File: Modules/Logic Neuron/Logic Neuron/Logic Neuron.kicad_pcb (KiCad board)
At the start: 2 copper layers, 123.1 x 128.5 mm, 122 parts, among them J1 PJ301M-12, J10 PJ301M-12, J11 EURO_PWR_2x5, J2 PJ301M-12, J3 PJ301M-12, J4 PJ301M-12, J5 Conn_01x04, J6 Conn_01x04, J7 PJ301M-12, J8 PJ301M-12, J9 PJ301M-12, U1 TL074, U2 LM339, U3 TL074, U4 TL074, U5 LM79L05_TO92, U9 LM339

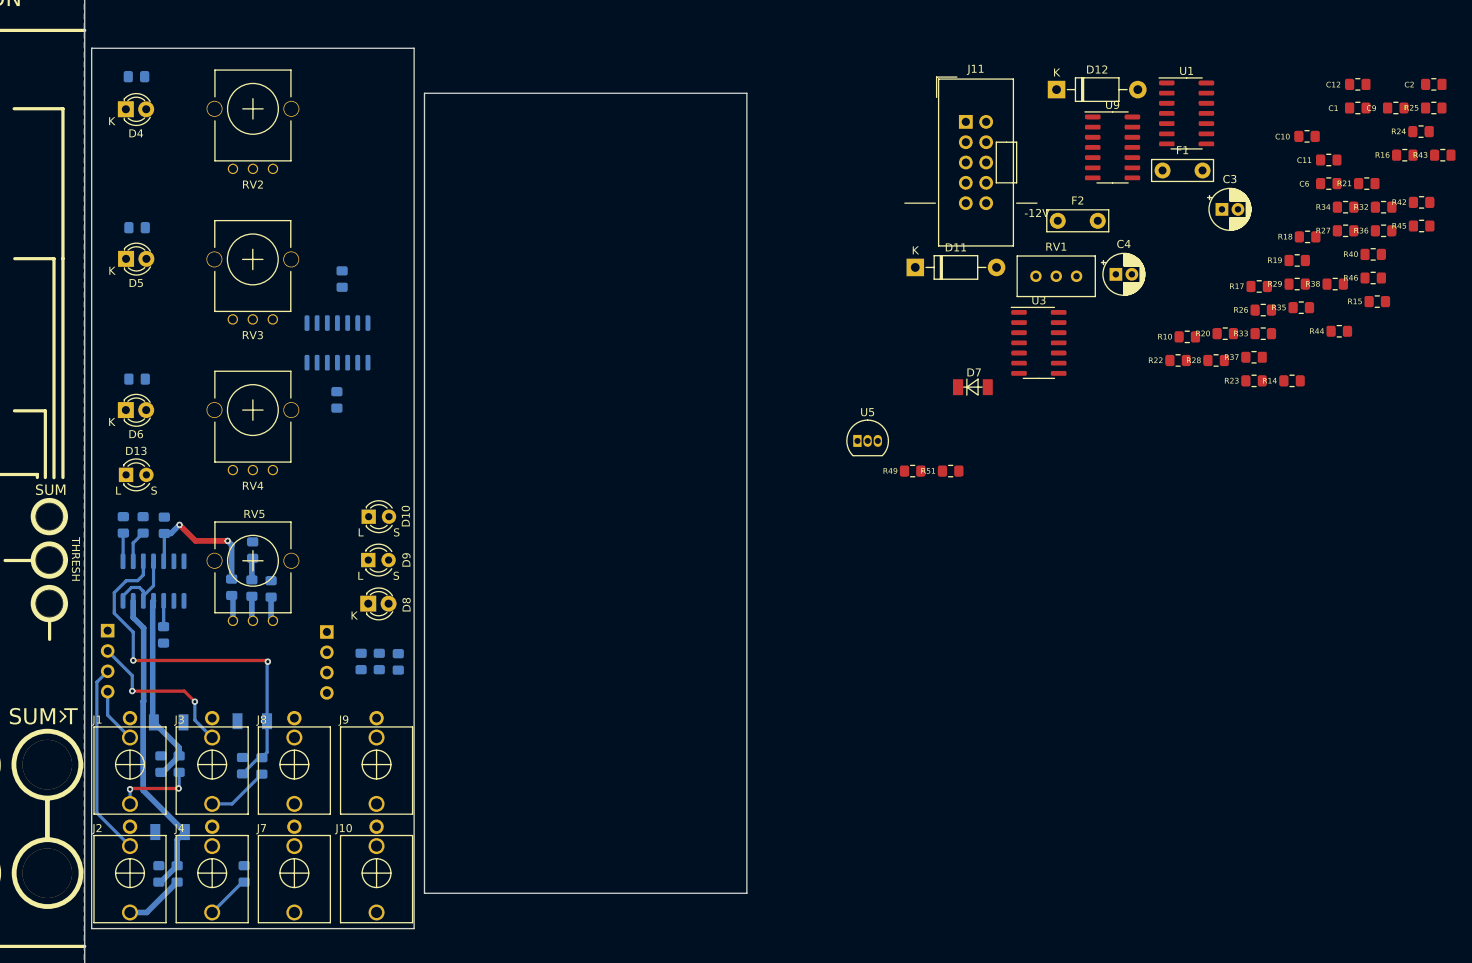
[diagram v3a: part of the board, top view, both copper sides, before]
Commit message: Logic Neuron : PCB routing
Logic Neuron: First pass of PCB routing almost completed.

To do:
- ground planes
- DRCs
- silkscreen markings
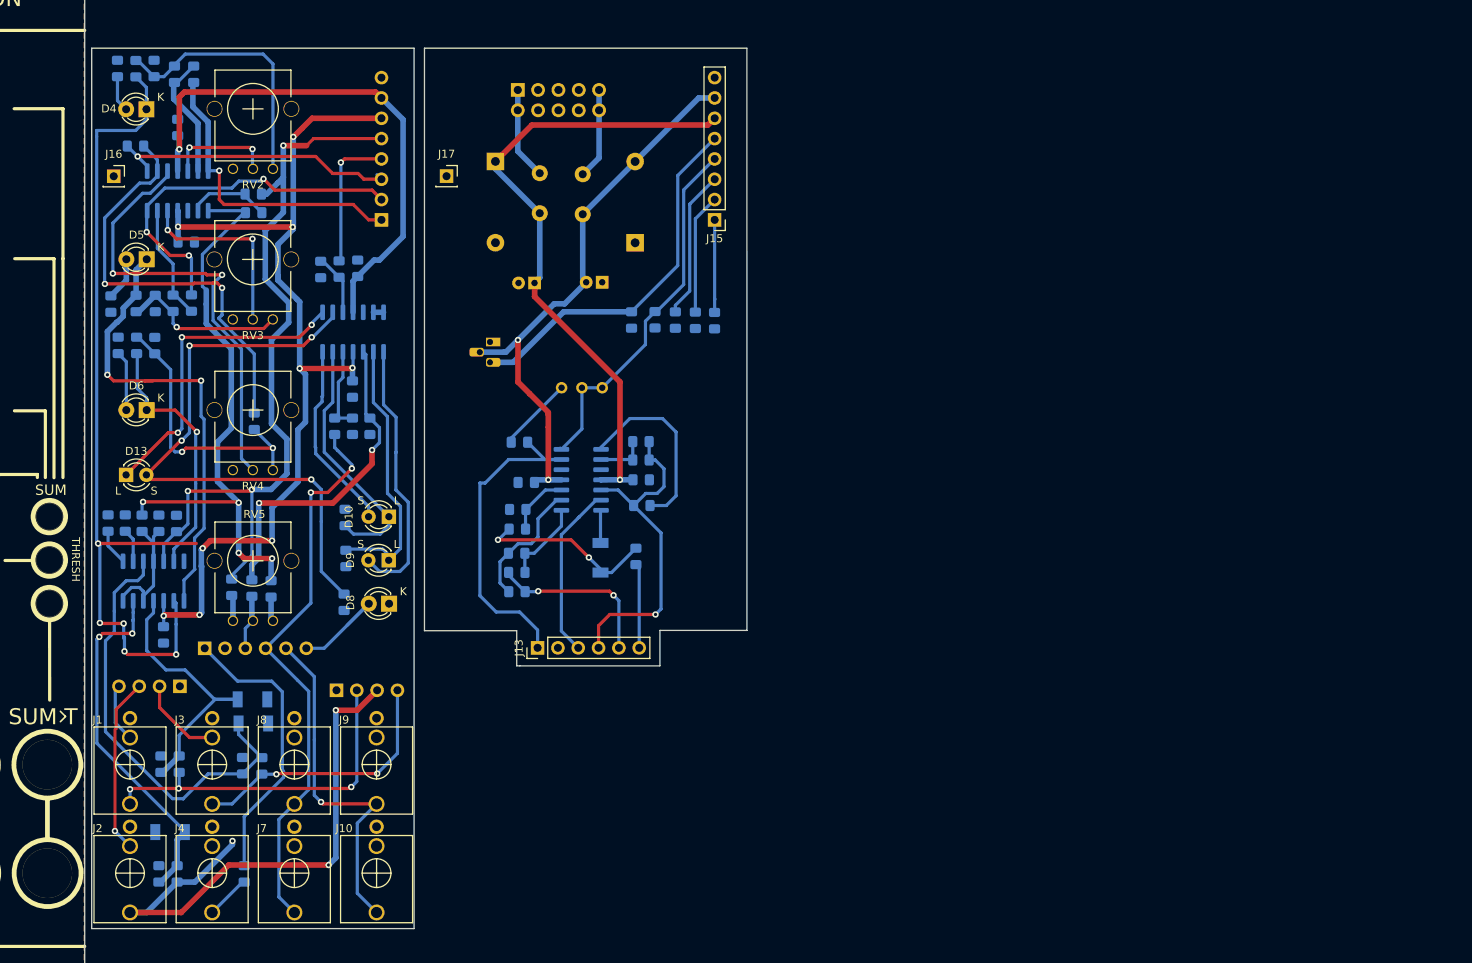
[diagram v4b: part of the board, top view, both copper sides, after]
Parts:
- removed U9: LM339, Package_SO:SOIC-14_3.9x8.7mm_P1.27mm
- added J12: Conn_01x06, Connector_PinHeader_2.54mm:PinHeader_1x06_P2.54mm_Vertical, B.Cu at (72.3, 103.6)
- added J13: Conn_01x06, Connector_PinHeader_2.54mm:PinHeader_1x06_P2.54mm_Vertical, F.Cu at (113.9, 103.6)
- added J14: Conn_01x08, Connector_PinHeader_2.54mm:PinHeader_1x08_P2.54mm_Vertical, B.Cu at (94.4, 50.1)
- added J15: Conn_01x08, Connector_PinHeader_2.54mm:PinHeader_1x08_P2.54mm_Vertical, F.Cu at (136.0, 50.1)
- added J16: Conn_01x01, Connector_PinSocket_2.54mm:PinSocket_1x01_P2.54mm_Vertical, F.Cu at (60.9, 44.6)
- added J17: Conn_01x01, Connector_PinSocket_2.54mm:PinSocket_1x01_P2.54mm_Vertical, F.Cu at (102.5, 44.6)
- C1, C10, C11, C12, C2, C3, C4, C6, C9, D11, D12, D7, F1, F2, J11, R10, R14, R15, R16, R17, R18, R19, R20, R21, R22, R23, R24, R25, R26, R27, R28, R29, R32, R33, R34, R35, R36, R37, R38, R40, R42, R43, R44, R45, R46, R49, R51, RV1, U1, U3: moved to B.Cu
- U5: footprint Package_TO_SOT_THT:TO-92_Inline -> Package_TO_SOT_THT:TO-92_HandSolder; moved to B.Cu
- moved R43 169.0 mm to (64.5, 88.0), turned to -90 degrees
- moved R25 162.4 mm to (63.6, 40.9), turned to 180 degrees
- moved R15 157.9 mm to (63.7, 31.2), turned to 90 degrees
- moved R16 157.3 mm to (66.1, 60.5), turned to -90 degrees
- moved R24 155.2 mm to (70.6, 60.5), turned to 90 degrees
- moved C9 152.1 mm to (70.0, 52.9), turned to 180 degrees
- moved R21 150.0 mm to (68.3, 60.5), turned to 90 degrees
- moved R44 149.5 mm to (66.5, 88.0), turned to 90 degrees
- moved R14 147.5 mm to (66.0, 31.1), turned to 90 degrees
- moved R45 146.1 mm to (78.3, 46.9)
- moved R19 145.5 mm to (63.8, 65.8), turned to 90 degrees
- moved R18 144.7 mm to (66.0, 65.8), turned to 90 degrees
- moved C10 141.2 mm to (68.9, 38.5), turned to 90 degrees
- moved R17 140.4 mm to (63.7, 60.5), turned to -90 degrees
- moved R46 140.2 mm to (78.4, 49.2)
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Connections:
- net V_threshold renamed V_threshold_f
- C1 pad 2: +SUM -> +SUM_b
- C6 pad 2: -5V_regulated -> -5V_regulated_b
- C8 pad 1: -5V_regulated -> -5V_regulated_f
- D8 pad 2: Net-(D8-Pad2) -> goutLED_f
- J10 pad 3: /gate_out -> gout_f
- J7 pad 3: +SUM -> +SUM_f
- J8 pad 3: +SUM -> +SUM_f
- J9 pad 3: /gate_out -> gout_f
- R10 pad 2: Net-(R10-Pad2) -> ch4_b
- R23 pad 2: -Analog_1 -> -Analog_1_f
- R24 pad 2: -Analog_2 -> -Analog_2_f
- R25 pad 2: -Analog_3 -> -Analog_3_f
- R26 pad 2: -Analog_1 -> -Analog_1_b
- R27 pad 2: -Analog_2 -> -Analog_2_b
- R28 pad 2: -Analog_3 -> -Analog_3_b
- R29 pad 2: -Analog_4 -> -Analog_4_b
- R30 pad 1: +5V_ref -> +5V_ref_f
- R31 pad 2: -5V_regulated -> -5V_regulated_f
- R32 pad 1: Net-(D8-Pad2) -> goutLED_b
- R35 pad 1: +SUM -> +SUM_b
- R36 pad 1: +SUM -> +SUM_b
- R37 pad 2: /gate_out -> gout_b
- R38 pad 2: /gate_out -> gout_b
- R4 pad 2: Net-(R10-Pad2) -> ch4_f
- R40 pad 1: +SUM -> +SUM_f
- R43 pad 1: +5V_ref -> +5V_ref_f
- R45 pad 2: -5V_regulated -> -5V_regulated_f
- R46 pad 1: +5V_ref -> +5V_ref_f
- R47 pad 1: Threshold -> Threshold_f
- R49 pad 1: -Analog_4 -> -Analog_4_f
- RV1 pad 1: -Analog_4 -> -Analog_4_b
- RV1 pad 2: -Analog_4 -> -Analog_4_b
- RV5 pad 2: Threshold -> Threshold_f
- U1 pad 1: -Analog_1 -> +5V_ref_f
- U1 pad 12: GND -> /Pot1
- U1 pad 13: Net-(R10-Pad2) -> Net-(R20-Pad2)
- U1 pad 14: -Analog_4 -> -Analog_1_f
- U1 pad 2: Net-(R20-Pad2) -> Net-(R45-Pad1)
- U1 pad 3: /Pot1 -> GND
- U1 pad 7: -Analog_2 -> -Analog_2_f
- U1 pad 8: -Analog_3 -> -Analog_3_f
- U2 pad 12: -5V_regulated -> -5V_regulated_f
- U3 pad 13: Net-(R45-Pad1) -> ch4_b
- U3 pad 14: +5V_ref -> -Analog_4_b
- U3 pad 5: +SUM -> +SUM_b
- U3 pad 6: Threshold -> Threshold_b
- U5 pad 3: -5V_regulated -> -5V_regulated_b
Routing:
- net +12V: track 3.23 -> 201.5 mm, vias 0 -> 10
- net -12V: track 0.00 -> 138.6 mm, vias 0 -> 3
- net Net-(D4-Pad1): track 0.00 -> 106.9 mm, vias 0 -> 5
- net -5V_regulated_f: track 0.00 -> 97.1 mm, vias 0 -> 3
- net Net-(U4-Pad9): track 0.00 -> 75.3 mm, vias 0 -> 4
- net +5V_ref_f: track 0.00 -> 73.9 mm, vias 0 -> 4
- net +SUM_f: track 0.00 -> 70.9 mm, vias 0 -> 2
- net in2: track 7.47 -> 70.0 mm, vias 0 -> 3
- net Net-(D5-Pad1): track 0.00 -> 58.2 mm, vias 0 -> 2
- net /Pot3: track 0.00 -> 56.8 mm, vias 0 -> 2
- net Net-(R22-Pad2): track 0.00 -> 54.1 mm, vias 0 -> 2
- net -Analog_2_f: track 0.00 -> 46.6 mm, vias 0 -> 3
- net -5V_regulated_b: track 0.00 -> 46.3 mm
- net -Analog_4_b: track 0.00 -> 46.1 mm
- net gout_f: track 0.00 -> 43.6 mm, vias 0 -> 1
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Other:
- outline, holes or cut-outs redrawn

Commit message: Logic neuron: PCB layout finished
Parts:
- J16: moved to B.Cu
- moved R40 0.56 mm to (88.5, 76.4)
- moved R42 0.56 mm to (90.7, 76.4), turned to 90 degrees
- moved R48 0.56 mm to (92.9, 76.4)
- turned J16 to 180 degrees
- turned R14 to -90 degrees
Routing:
- net GND: track 0.00 -> 103.4 mm, vias 0 -> 13
- net Net-(C1-Pad1): track 6.29 -> 35.1 mm
- net Net-(D4-Pad1): track 106.9 -> 94.4 mm, vias 5 -> 4
- net in2: track 70.0 -> 60.7 mm, vias 3 -> 2
- net goutLED_f: track 13.9 -> 10.1 mm
- net ch4_f: track 35.8 -> 38.5 mm
- net +SUM_b: track 42.3 -> 44.9 mm, vias 1 -> 3
- net ch4_b: track 41.8 -> 44.2 mm, vias 0 -> 2
- net Net-(R36-Pad2): track 23.5 -> 25.9 mm, vias 0 -> 2
- net /Pot3: track 56.8 -> 58.8 mm
- net Net-(R40-Pad2): track 10.9 -> 12.3 mm
- net Net-(R14-Pad1): track 32.9 -> 31.8 mm
- net Net-(D5-Pad1): track 58.2 -> 57.3 mm
- net -Analog_3_f: track 36.6 -> 35.8 mm
- net norm_in3: track 11.4 -> 10.8 mm
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- added copper zone on B.Cu, net (none)
- added copper zone on F.Cu, net (none)
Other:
- board text added: "Daisy chain Input"
- board text added: "Daisy chain Output"
- board text added: "JLCJLCJLCJLC"
- board text added: "Material Mathods Logic Neuron v1 Sam Tusk 2022"
- board text added: "Trim for 1x amplificaiton of Ch4 in Mix out"
